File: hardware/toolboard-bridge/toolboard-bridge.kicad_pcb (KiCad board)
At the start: 2 copper layers, 50 x 30 mm, 47 parts, among them J1 USB-C 16P, J2 MF3 2x04P, J3 1x2P, J4 2P 9.5mm, J5 1x3P, K1 12V SRD-C, Q1 2N7002, Q2 2N7002, Q3 MMBT3904, U1 TPS54335A, U2 LTV-357T, U4 USBLC6-2SC6

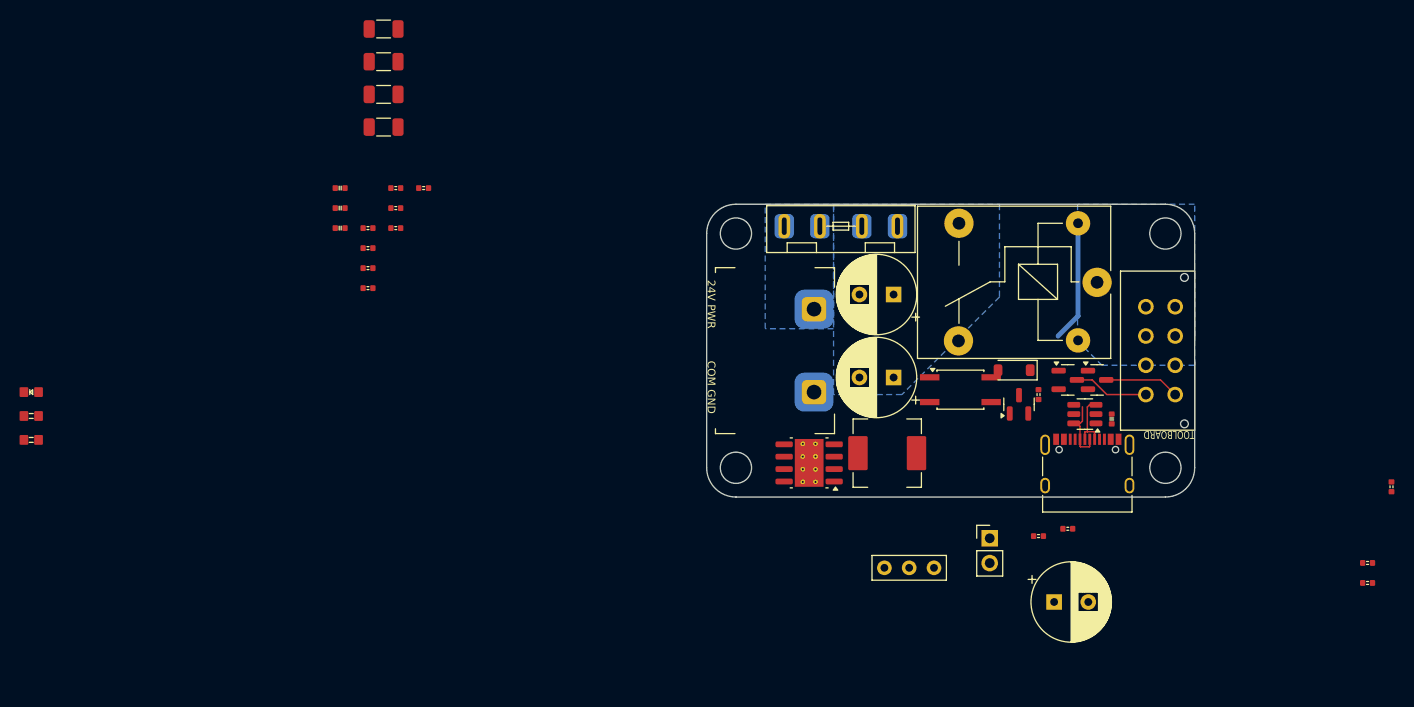
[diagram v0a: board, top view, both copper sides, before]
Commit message: cleaned up corevus toolboard schematics to be more presentable
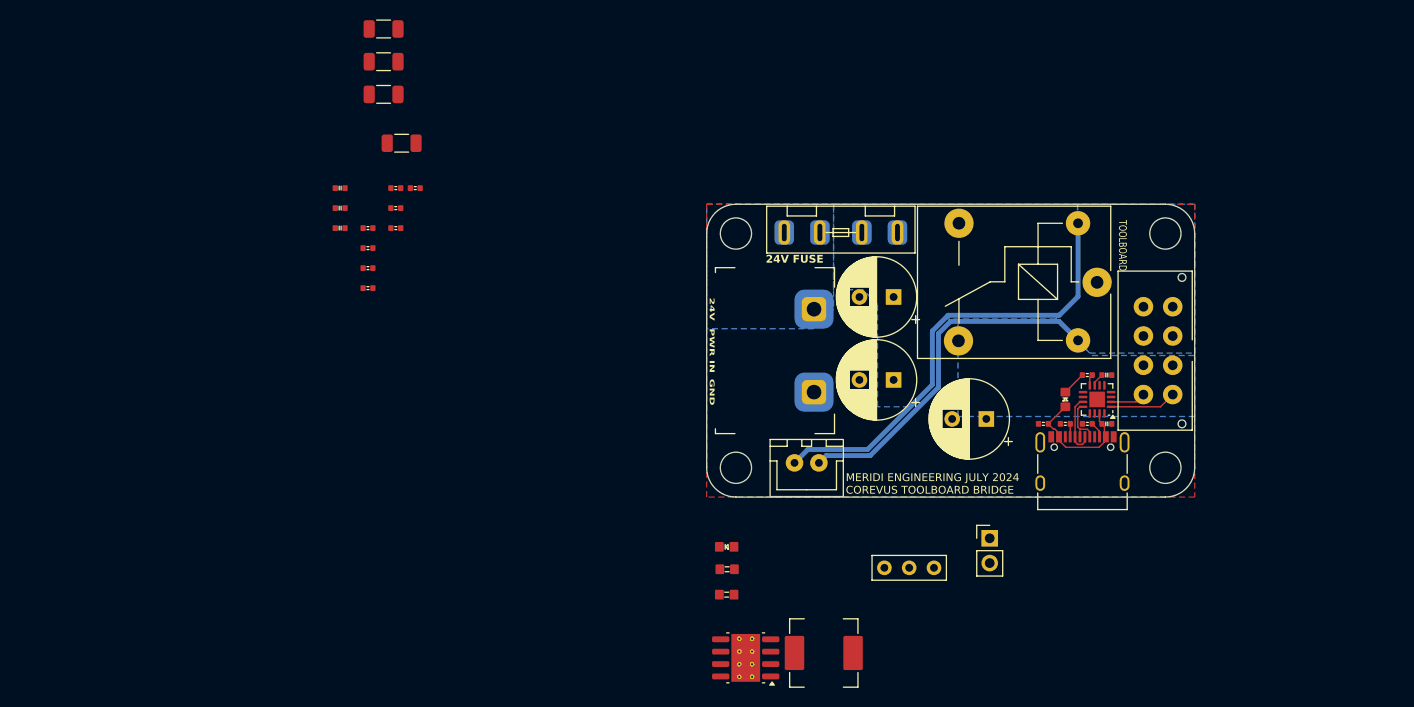
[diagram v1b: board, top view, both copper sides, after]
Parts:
- removed Q1, Q2: 2N7002, Package_TO_SOT_SMD:SOT-23
- removed Q3: MMBT3904, Package_TO_SOT_SMD:SOT-23
- removed R15, R16: 1kΩ, PCM_ME_passives:0402R
- removed U4: USBLC6-2SC6, Package_TO_SOT_SMD:SOT-23-6
- added C11: 1μF, PCM_ME_passives:0402C, F.Cu at (156.0, 72.5)
- added J6: XH 1x2P, corevus:JST_XH_1x02, F.Cu at (125.2, 76.5)
- C12: value 1μF -> 100nF 25V
- D2: value ??? -> Red; footprint Diode_SMD:D_SOD-123 -> PCM_ME_passives:0603LED
- R10: value 2.2kΩ -> 1kΩ
- U2: value LTV-357T -> DPO2039; footprint Package_SO:SO-4_4.4x3.6mm_P2.54mm -> Package_DFN_QFN:VQFN-16-1EP_3x3mm_P0.5mm_EP1.6x1.6mm
- moved R5 73.0 mm to (117.1, 87.4)
- moved D1 73.0 mm to (117.0, 85.1)
- moved R6 73.0 mm to (117.0, 90.0)
- moved R14 36.1 mm to (149.5, 72.5)
- moved L1 21.5 mm to (127.0, 96.0)
- moved U1 21.0 mm to (119.0, 96.5)
- moved C7 20.0 mm to (143.7, 72.0), turned to 180 degrees
- moved U2 14.0 mm to (155.0, 70.0), turned to 180 degrees
- moved R12 12.5 mm to (154.0, 72.5), turned to 180 degrees
- moved R11 10.8 mm to (151.8, 72.5), turned to 180 degrees
- moved D2 6.05 mm to (151.8, 70.0), turned to -90 degrees
- moved R10 5.39 mm to (154.0, 67.5), turned to 0 degrees
- moved C12 4.53 mm to (156.0, 67.5), turned to 180 degrees
- moved C10 2.48 mm to (83.8, 43.8)
- moved R13 0.85 mm to (85.2, 48.4)
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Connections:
- C12 pad 1: +5V -> GND
- C12 pad 2: GND -> Net-(U2-CB)
- D2 pad 1: +12V -> Net-(D2-K)
- D2 pad 2: Net-(D2-A) -> +5V
- F1 pad 1: +24V -> Net-(J4-Pin_1)
- F1 pad 2: Net-(J4-Pin_1) -> +24V
- K1 pad 2: Net-(D2-A) -> Net-(J6-Pin_1)
- K1 pad 5: +12V -> Net-(J6-Pin_2)
- R10 pad 1: Net-(R10-Pad1) -> Net-(D2-K)
- R10 pad 2: Net-(Q3-B) -> Net-(U2-FAULTB)
- U2 pad 1: unconnected-(U2-Pad1) -> /TB_D+
- U2 pad 2: unconnected-(U2-Pad2) -> /TB_D-
- U2 pad 3: Net-(R10-Pad1) -> GND
- U2 pad 4: +12V -> GND
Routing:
- net Net-(J6-Pin_1): track 0.00 -> 46.8 mm
- net Net-(J6-Pin_2): track 0.00 -> 36.6 mm
- net +5V: track 0.00 -> 12.9 mm
- net Net-(D2-A): track 12.4 -> 0.00 mm
- net /TB_D-: track 7.68 -> 3.62 mm
- net Net-(D2-K): track 0.00 -> 2.47 mm
- net Net-(J1-CC2): track 0.00 -> 1.64 mm
- net Net-(U2-CB): track 0.00 -> 1.37 mm
- net Net-(J1-CC1): track 0.00 -> 1.33 mm
- net Net-(U2-FAULTB): track 0.00 -> 1.17 mm
- net /USB_D+: track 6.00 -> 4.90 mm
- net /TB_D+: track 7.68 -> 6.83 mm
- net /USB_D-: track 6.63 -> 6.04 mm
- added copper zone on B.Cu, net +12V
- added copper zone on F.Cu, net GND
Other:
- board text added: "24V"
- board text added: "24V FUSE"
- board text added: "GND"
- board text added: "MERIDI ENGINEERING JULY 2024 COREVUS TOOLBOARD BRIDGE"
- board text added: "PWR IN"
- board text removed: "24V PWR"
- board text removed: "COM GND"
